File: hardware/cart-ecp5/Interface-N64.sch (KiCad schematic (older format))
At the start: 1 part

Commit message: Add basic N64 interface with UltraCIC II
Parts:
- added J?: Conn_01x05, symbol Connector_Generic:Conn_01x05
- added R?: 10k, symbol Device:R
- added RN4, RN5, RN6, RN7, RN8, RN9: 33R, 1%, Resistor_SMD:R_Array_Convex_4x0603, symbol Device:R_Pack04
- added U?: ATtiny25-20SU, Package_SO:SOIJ-8_5.3x5.3mm_P1.27mm, symbol MCU_Microchip_ATtiny:ATtiny25-20SU
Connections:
- net labels added: CIC_MISO, CIC_MOSI, CIC_RESET#, CIC_SCK, N64_CIC_DATA1, N64_CIC_DATA2, P3V3, xN64_AD0, xN64_AD1, xN64_AD10, xN64_AD11, xN64_AD12, xN64_AD13, xN64_AD14, xN64_AD15, xN64_AD2, xN64_AD3, xN64_AD4, xN64_AD5, xN64_AD6, xN64_AD7, xN64_AD8, xN64_AD9, xN64_ALE_H, xN64_ALE_L, xN64_COLD_RESET#, xN64_OS_EVENT#, xN64_READ#, xN64_WRITE#
- net labels removed: N64_12V, N64_AUDIO_L, N64_AUDIO_R, N64_S_DAT
- wire segments 64 -> 96
- no-connect marks 0 -> 10
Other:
- moved on the sheet: J?

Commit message: First pass annotation and footprint assignment complete
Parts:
- J4: renamed from J?; footprint (none) -> Connector_PinHeader_2.54mm:PinHeader_1x05_P2.54mm_Vertical
- R6: renamed from R?; footprint (none) -> Resistor_SMD:R_0603_1608Metric
- gave numbers to parts that had none: 2
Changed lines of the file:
@@
 $EndDescr
 $Comp
-L ng_n64:N64_Cartridge_Bus J?
+L ng_n64:N64_Cartridge_Bus J3
 U 1 1 5F443545
 P 3000 4050
-F 0 "J?" H 2450 5800 60  0000 L CNN
+F 0 "J3" H 2450 5800 60  0000 L CNN
 F 1 "N64_Cartridge_Bus" H 2450 2300 60  0000 L CNN
 F 2 "ng_n64:N64_Cartridge_Edge" H 3600 550 60  0001 C CNN
@@
 xN64_ALE_H
 $Comp
-L MCU_Microchip_ATtiny:ATtiny25-20SU U?
+L MCU_Microchip_ATtiny:ATtiny25-20SU U4
 U 1 1 5F5E9784
 P 7450 4950
-F 0 "U?" H 6921 4996 50  0000 R CNN
+F 0 "U4" H 6921 4996 50  0000 R CNN
 F 1 "ATtiny25-20SU" H 6921 4905 50  0000 R CNN
 F 2 "Package_SO:SOIJ-8_5.3x5.3mm_P1.27mm" H 7450 4950 50  0001 C CIN
@@
 	7450 5550 7450 5650
 $Comp
-L ng_power:GND #PWR?
+L ng_power:GND #PWR013
 U 1 1 5F5EFD38
 P 2200 5750
-F 0 "#PWR?" H 2200 5500 50  0001 C CNN
+F 0 "#PWR013" H 2200 5500 50  0001 C CNN
 F 1 "GND" H 2203 5624 50  0000 C CNN
 F 2 "" H 2100 5400 50  0001 C CNN
@@
 $EndComp
 $Comp
-L ng_power:GND #PWR?
+L ng_power:GND #PWR015
 U 1 1 5F5F0698
 P 7450 5650
-F 0 "#PWR?" H 7450 5400 50  0001 C CNN
+F 0 "#PWR015" H 7450 5400 50  0001 C CNN
 F 1 "GND" H 7453 5524 50  0000 C CNN
 F 2 "" H 7350 5300 50  0001 C CNN
@@
 	6750 4650 6750 5250
 $Comp
-L ng_power:GND #PWR?
+L ng_power:GND #PWR014
 U 1 1 5F607950
 P 6750 5650
-F 0 "#PWR?" H 6750 5400 50  0001 C CNN
+F 0 "#PWR014" H 6750 5400 50  0001 C CNN
 F 1 "GND" H 6753 5524 50  0000 C CNN
 F 2 "" H 6650 5300 50  0001 C CNN
@@
 CIC_MISO
 $Comp
-L Device:R R?
+L Device:R R6
 U 1 1 5F61BC6C
 P 6750 5400
-F 0 "R?" H 6680 5354 50  0000 R CNN
+F 0 "R6" H 6680 5354 50  0000 R CNN
 F 1 "10k" H 6680 5445 50  0000 R CNN
-F 2 "" V 6680 5400 50  0001 C CNN
+F 2 "Resistor_SMD:R_0603_1608Metric" V 6680 5400 50  0001 C CNN
 F 3 "~" H 6750 5400 50  0001 C CNN
 	1    6750 5400
@@
 NoConn ~ 6850 5050
 $Comp
-L Connector_Generic:Conn_01x05 J?
+L Connector_Generic:Conn_01x05 J4
 U 1 1 5F631439
 P 9700 4950
-F 0 "J?" H 9780 4992 50  0000 L CNN
+F 0 "J4" H 9780 4992 50  0000 L CNN
 F 1 "Conn_01x05" H 9780 4901 50  0000 L CNN
-F 2 "" H 9700 4950 50  0001 C CNN
+F 2 "Connector_PinHeader_2.54mm:PinHeader_1x05_P2.54mm_Vertical" H 9700 4950 50  0001 C CNN
 F 3 "~" H 9700 4950 50  0001 C CNN
 	1    9700 4950
@@
 	9400 4750 9400 5250
 $Comp
-L ng_power:GND #PWR?
+L ng_power:GND #PWR016
 U 1 1 5F634AA1
 P 9400 5250
-F 0 "#PWR?" H 9400 5000 50  0001 C CNN
+F 0 "#PWR016" H 9400 5000 50  0001 C CNN
 F 1 "GND" H 9403 5124 50  0000 C CNN
 F 2 "" H 9300 4900 50  0001 C CNN

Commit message: Initial placement pass
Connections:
- net N64_AD0: now also RN4.5 (R4.2); no longer RN4.7 (R2.2)
- net N64_AD1: now also RN4.7 (R2.2); no longer RN4.5 (R4.2)
- net N64_AD10: now also RN5.8 (R1.2); no longer RN5.6 (R3.2)
- net N64_AD11: now also RN5.6 (R3.2); no longer RN5.8 (R1.2)
- net N64_AD12: now also RN6.8 (R1.2); no longer RN6.6 (R3.2)
- net N64_AD13: now also RN6.6 (R3.2); no longer RN6.8 (R1.2)
- net N64_AD14: now also RN4.8 (R1.2); no longer RN4.6 (R3.2)
- net N64_AD15: now also RN4.6 (R3.2); no longer RN4.8 (R1.2)
- net N64_AD2: now also RN6.5 (R4.2); no longer RN6.7 (R2.2)
- net N64_AD3: now also RN6.7 (R2.2); no longer RN6.5 (R4.2)
- net N64_AD4: now also RN5.5 (R4.2); no longer RN5.7 (R2.2)
- net N64_AD5: now also RN5.7 (R2.2); no longer RN5.5 (R4.2)
- net N64_AD6: now also RN7.5 (R4.2); no longer RN7.7 (R2.2)
- net N64_AD7: now also RN7.7 (R2.2); no longer RN7.5 (R4.2)
- net N64_AD8: now also RN7.8 (R1.2); no longer RN7.6 (R3.2)
- net N64_AD9: now also RN7.6 (R3.2); no longer RN7.8 (R1.2)
- net N64_ALE_H: now also RN8.7 (R2.2); no longer RN8.5 (R4.2)
- net N64_ALE_L: now also RN8.5 (R4.2); no longer RN8.8 (R1.2)
- net N64_OS_EVENT#: now also RN9.6 (R3.2); no longer RN9.8 (R1.2)
- net N64_READ#: now also RN8.8 (R1.2); no longer RN8.6 (R3.2)
- net N64_S_CLK: now also RN9.5 (R4.2); no longer J3.19 (S_CLK)
- net N64_WRITE#: now also RN8.6 (R3.2); no longer RN8.7 (R2.2)
- net xN64_AD0: now also RN4.4 (R4.1); no longer RN4.2 (R2.1)
- net xN64_AD1: now also RN4.2 (R2.1); no longer RN4.4 (R4.1)
- net xN64_AD10: now also RN5.1 (R1.1); no longer RN5.3 (R3.1)
- net xN64_AD11: now also RN5.3 (R3.1); no longer RN5.1 (R1.1)
- net xN64_AD12: now also RN6.1 (R1.1); no longer RN6.3 (R3.1)
- net xN64_AD13: now also RN6.3 (R3.1); no longer RN6.1 (R1.1)
- net xN64_AD14: now also RN4.1 (R1.1); no longer RN4.3 (R3.1)
- net xN64_AD15: now also RN4.3 (R3.1); no longer RN4.1 (R1.1)
- net xN64_AD2: now also RN6.4 (R4.1); no longer RN6.2 (R2.1)
- net xN64_AD3: now also RN6.2 (R2.1); no longer RN6.4 (R4.1)
- net xN64_AD4: now also RN5.4 (R4.1); no longer RN5.2 (R2.1)
- net xN64_AD5: now also RN5.2 (R2.1); no longer RN5.4 (R4.1)
- net xN64_AD6: now also RN7.4 (R4.1); no longer RN7.2 (R2.1)
- net xN64_AD7: now also RN7.2 (R2.1); no longer RN7.4 (R4.1)
- net xN64_AD8: now also RN7.1 (R1.1); no longer RN7.3 (R3.1)
- net xN64_AD9: now also RN7.3 (R3.1); no longer RN7.1 (R1.1)
- net xN64_ALE_H: now also RN8.2 (R2.1); no longer RN8.4 (R4.1)
- net xN64_ALE_L: now also RN8.4 (R4.1); no longer RN8.1 (R1.1)
- net xN64_OS_EVENT#: now also RN9.3 (R3.1); no longer RN9.1 (R1.1)
- net xN64_READ#: now also RN8.1 (R1.1); no longer RN8.3 (R3.1)
- net xN64_WRITE#: now also RN8.3 (R3.1); no longer RN8.2 (R2.1)
- net xN64_S_CLK: now reaches RN9.4 (R4.1)
- net xN64_S_CLK: now also J3.19 (S_CLK)
- net xN64_S_DAT: now reaches J3.21 (S_DAT)
- net xN64_S_DAT: now also RN9.1 (R1.1)
- new net N64_S_DAT: RN9.8 (R1.2)
- no-connect marks 10 -> 5
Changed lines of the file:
@@
 AR Path="/5F1CD155" Ref="RN?"  Part="1"
 AR Path="/5F133F50/5F1CD155" Ref="RN4"  Part="1"
-AR Path="/5F43B1FD/5F1CD155" Ref="RN4"  Part="1"
-F 0 "RN4" V 6683 2100 50  0000 C CNN
+AR Path="/5F43B1FD/5F1CD155" Ref="RN1"  Part="1"
+F 0 "RN1" V 6683 2100 50  0000 C CNN
 F 1 "33R, 1%" V 6774 2100 50  0000 C CNN
 F 2 "Resistor_SMD:R_Array_Convex_4x0603" V 7375 2100 50  0001 C CNN
@@
 AR Path="/5F1CD15B" Ref="RN?"  Part="1"
 AR Path="/5F133F50/5F1CD15B" Ref="RN6"  Part="1"
-AR Path="/5F43B1FD/5F1CD15B" Ref="RN6"  Part="1"
-F 0 "RN6" V 6683 2800 50  0000 C CNN
+AR Path="/5F43B1FD/5F1CD15B" Ref="RN2"  Part="1"
+F 0 "RN2" V 6683 2800 50  0000 C CNN
 F 1 "33R, 1%" V 6774 2800 50  0000 C CNN
 F 2 "Resistor_SMD:R_Array_Convex_4x0603" V 7375 2800 50  0001 C CNN
@@
 AR Path="/5F1CD161" Ref="RN?"  Part="1"
 AR Path="/5F133F50/5F1CD161" Ref="RN8"  Part="1"
-AR Path="/5F43B1FD/5F1CD161" Ref="RN8"  Part="1"
-F 0 "RN8" V 6683 3500 50  0000 C CNN
+AR Path="/5F43B1FD/5F1CD161" Ref="RN3"  Part="1"
+F 0 "RN3" V 6683 3500 50  0000 C CNN
 F 1 "33R, 1%" V 6774 3500 50  0000 C CNN
 F 2 "Resistor_SMD:R_Array_Convex_4x0603" V 7375 3500 50  0001 C CNN
@@
 AR Path="/5F1CD167" Ref="RN?"  Part="1"
 AR Path="/5F133F50/5F1CD167" Ref="RN5"  Part="1"
-AR Path="/5F43B1FD/5F1CD167" Ref="RN5"  Part="1"
-F 0 "RN5" V 8533 2100 50  0000 C CNN
+AR Path="/5F43B1FD/5F1CD167" Ref="RN4"  Part="1"
+F 0 "RN4" V 8533 2100 50  0000 C CNN
 F 1 "33R, 1%" V 8624 2100 50  0000 C CNN
 F 2 "Resistor_SMD:R_Array_Convex_4x0603" V 9225 2100 50  0001 C CNN
@@
 AR Path="/5F1CD16D" Ref="RN?"  Part="1"
 AR Path="/5F133F50/5F1CD16D" Ref="RN7"  Part="1"
-AR Path="/5F43B1FD/5F1CD16D" Ref="RN7"  Part="1"
-F 0 "RN7" V 8533 2800 50  0000 C CNN
+AR Path="/5F43B1FD/5F1CD16D" Ref="RN5"  Part="1"
+F 0 "RN5" V 8533 2800 50  0000 C CNN
 F 1 "33R, 1%" V 8624 2800 50  0000 C CNN
 F 2 "Resistor_SMD:R_Array_Convex_4x0603" V 9225 2800 50  0001 C CNN
@@
 AR Path="/5F1CD183" Ref="RN?"  Part="1"
 AR Path="/5F133F50/5F1CD183" Ref="RN9"  Part="1"
-AR Path="/5F43B1FD/5F1CD183" Ref="RN9"  Part="1"
-F 0 "RN9" V 8533 3500 50  0000 C CNN
+AR Path="/5F43B1FD/5F1CD183" Ref="RN6"  Part="1"
+F 0 "RN6" V 8533 3500 50  0000 C CNN
 F 1 "33R, 1%" V 8624 3500 50  0000 C CNN
 F 2 "Resistor_SMD:R_Array_Convex_4x0603" V 9225 3500 50  0001 C CNN
@@
 	0    1    1    0
 $EndComp
+Text GLabel 7300 2200 2    50   Input ~ 0
+N64_AD0
+Text GLabel 7300 2100 2    50   Input ~ 0
+N64_AD15
+Text GLabel 7300 1900 2    50   Input ~ 0
+N64_AD14
 Text GLabel 7300 2000 2    50   Input ~ 0
-N64_AD0
-Text GLabel 7300 1900 2    50   Input ~ 0
-N64_AD15
-Text GLabel 7300 2100 2    50   Input ~ 0
-N64_AD14
-Text GLabel 7300 2200 2    50   Input ~ 0
 N64_AD1
+Text GLabel 7300 2900 2    50   Input ~ 0
+N64_AD2
 Text GLabel 7300 2700 2    50   Input ~ 0
-N64_AD2
-Text GLabel 7300 2900 2    50   Input ~ 0
 N64_AD3
+Text GLabel 7300 3600 2    50   Input ~ 0
+N64_ALE_L
+Text GLabel 7300 3400 2    50   Input ~ 0
+N64_ALE_H
+Text GLabel 7300 3500 2    50   Input ~ 0
+N64_WRITE#
 Text GLabel 7300 3300 2    50   Input ~ 0
-N64_ALE_L
-Text GLabel 7300 3600 2    50   Input ~ 0
-N64_ALE_H
-Text GLabel 7300 3400 2    50   Input ~ 0
-N64_WRITE#
-Text GLabel 7300 3500 2    50   Input ~ 0
 N64_READ#
+Text GLabel 7300 2800 2    50   Input ~ 0
+N64_AD13
 Text GLabel 7300 2600 2    50   Input ~ 0
-N64_AD13
-Text GLabel 7300 2800 2    50   Input ~ 0
 N64_AD12
+Text GLabel 9150 2100 2    50   Input ~ 0
+N64_AD11
 Text GLabel 9150 1900 2    50   Input ~ 0
-N64_AD11
-Text GLabel 9150 2100 2    50   Input ~ 0
 N64_AD10
+Text GLabel 9150 2800 2    50   Input ~ 0
+N64_AD9
 Text GLabel 9150 2600 2    50   Input ~ 0
-N64_AD9
-Text GLabel 9150 2800 2    50   Input ~ 0
 N64_AD8
 Text GLabel 9150 3400 2    50   Input ~ 0
 N64_COLD_RESET#
 Text GLabel 9150 3300 2    50   Input ~ 0
-N64_OS_EVENT#
+N64_S_DAT
+Text GLabel 9150 2200 2    50   Input ~ 0
+N64_AD4
 Text GLabel 9150 2000 2    50   Input ~ 0
-N64_AD4
-Text GLabel 9150 2200 2    50   Input ~ 0
 N64_AD5
+Text GLabel 9150 2900 2    50   Input ~ 0
+N64_AD6
 Text GLabel 9150 2700 2    50   Input ~ 0
-N64_AD6
-Text GLabel 9150 2900 2    50   Input ~ 0
 N64_AD7
-NoConn ~ 8750 3600
-NoConn ~ 8750 3500
-NoConn ~ 9150 3500
-NoConn ~ 9150 3600
 NoConn ~ 3700 5550
 NoConn ~ 3700 5650
@@
 xN64_WRITE#
 Text Label 3800 4750 0    50   ~ 0
-N64_S_CLK
+xN64_S_CLK
 Text Label 3800 4950 0    50   ~ 0
 xN64_COLD_RESET#
@@
 Text Label 3800 5350 0    50   ~ 0
 N64_CIC_DATA2
-NoConn ~ 3700 4650
 NoConn ~ 2300 2950
 NoConn ~ 2300 3050
@@
 Wire Wire Line
 	6900 3600 6800 3600
+Text Label 6800 2100 2    50   ~ 0
+xN64_AD15
+Text Label 6800 2200 2    50   ~ 0
+xN64_AD0
 Text Label 6800 1900 2    50   ~ 0
-xN64_AD15
+xN64_AD14
 Text Label 6800 2000 2    50   ~ 0
-xN64_AD0
-Text Label 6800 2100 2    50   ~ 0
-xN64_AD14
-Text Label 6800 2200 2    50   ~ 0
 xN64_AD1
+Text Label 6800 2800 2    50   ~ 0
+xN64_AD13
+Text Label 6800 2900 2    50   ~ 0
+xN64_AD2
 Text Label 6800 2600 2    50   ~ 0
-xN64_AD13
+xN64_AD12
 Text Label 6800 2700 2    50   ~ 0
-xN64_AD2
-Text Label 6800 2800 2    50   ~ 0
-xN64_AD12
-Text Label 6800 2900 2    50   ~ 0
 xN64_AD3
+Text Label 8650 2100 2    50   ~ 0
+xN64_AD11
+Text Label 8650 2200 2    50   ~ 0
+xN64_AD4
 Text Label 8650 1900 2    50   ~ 0
-xN64_AD11
+xN64_AD10
 Text Label 8650 2000 2    50   ~ 0
-xN64_AD4
-Text Label 8650 2100 2    50   ~ 0
-xN64_AD10
-Text Label 8650 2200 2    50   ~ 0
 xN64_AD5
 Wire Wire Line
@@
 Wire Wire Line
 	8750 3400 8650 3400
+Text Label 8650 2900 2    50   ~ 0
+xN64_AD6
+Text Label 8650 2800 2    50   ~ 0
+xN64_AD9
 Text Label 8650 2700 2    50   ~ 0
-xN64_AD6
+xN64_AD7
 Text Label 8650 2600 2    50   ~ 0
-xN64_AD9
-Text Label 8650 2900 2    50   ~ 0
-xN64_AD7
-Text Label 8650 2800 2    50   ~ 0
 xN64_AD8
-Text Label 8650 3300 2    50   ~ 0
+Text Label 8650 3500 2    50   ~ 0
 xN64_OS_EVENT#
 Text Label 8650 3400 2    50   ~ 0
 xN64_COLD_RESET#
+Text Label 6800 3600 2    50   ~ 0
+xN64_ALE_L
+Text Label 6800 3500 2    50   ~ 0
+xN64_WRITE#
 Text Label 6800 3300 2    50   ~ 0
-xN64_ALE_L
+xN64_READ#
 Text Label 6800 3400 2    50   ~ 0
-xN64_WRITE#
-Text Label 6800 3500 2    50   ~ 0
-xN64_READ#
-Text Label 6800 3600 2    50   ~ 0
 xN64_ALE_H
 $Comp
@@
 Text Label 6100 4750 2    50   ~ 0
 N64_CIC_DATA2
-Text Label 6100 4950 2    50   ~ 0
-N64_S_CLK
 Text Label 6100 4850 2    50   ~ 0
 N64_CIC_DATA1
@@
 Text Label 9300 5150 2    50   ~ 0
 CIC_RESET#
+Wire Wire Line
+	3700 4650 3800 4650
+Text Label 3800 4650 0    50   ~ 0
+xN64_S_DAT
+Wire Wire Line
+	8750 3500 8650 3500
+Wire Wire Line
+	8750 3600 8650 3600
+Text GLabel 9150 3600 2    50   Input ~ 0
+N64_S_CLK
+Text GLabel 9150 3500 2    50   Input ~ 0
+N64_OS_EVENT#
+Text Label 8650 3300 2    50   ~ 0
+xN64_S_DAT
+Text Label 8650 3600 2    50   ~ 0
+xN64_S_CLK
+Text GLabel 6100 4950 0    50   Input ~ 0
+N64_S_CLK
 $EndSCHEMATC

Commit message: Shrink smallest passive to 0402
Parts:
- R6: footprint Resistor_SMD:R_0603_1608Metric -> Resistor_SMD:R_0402_1005Metric
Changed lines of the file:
@@
 F 0 "R6" H 6680 5354 50  0000 R CNN
 F 1 "10k" H 6680 5445 50  0000 R CNN
-F 2 "Resistor_SMD:R_0603_1608Metric" V 6680 5400 50  0001 C CNN
+F 2 "Resistor_SMD:R_0402_1005Metric" V 6680 5400 50  0001 C CNN
 F 3 "~" H 6750 5400 50  0001 C CNN
 	1    6750 5400

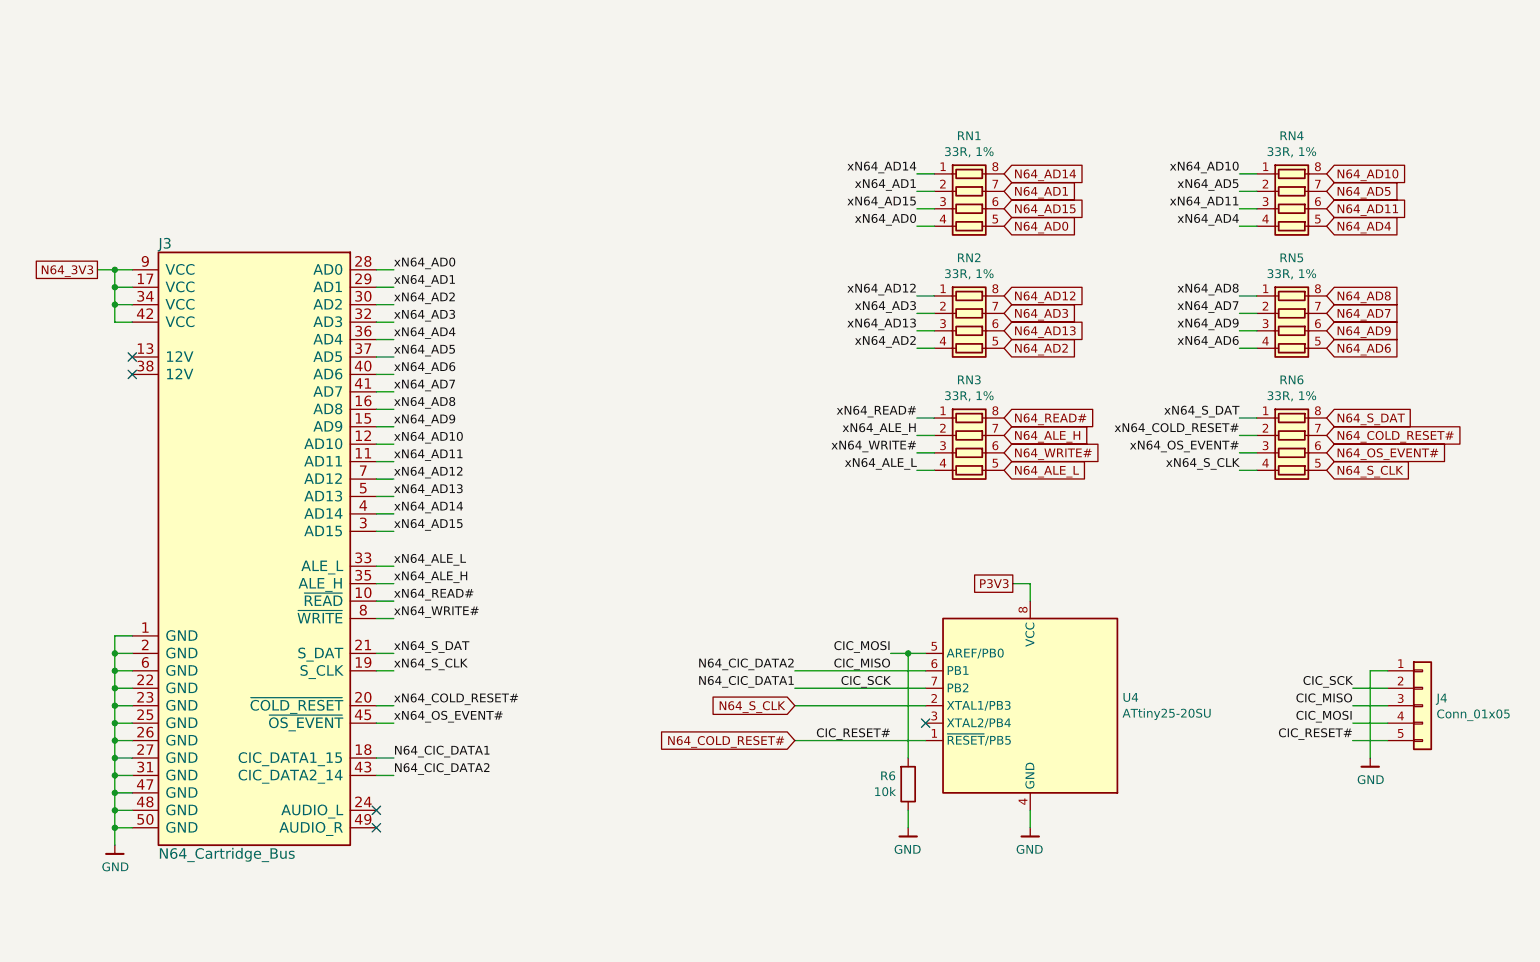
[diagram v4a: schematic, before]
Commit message: Refine placement to make room for power management
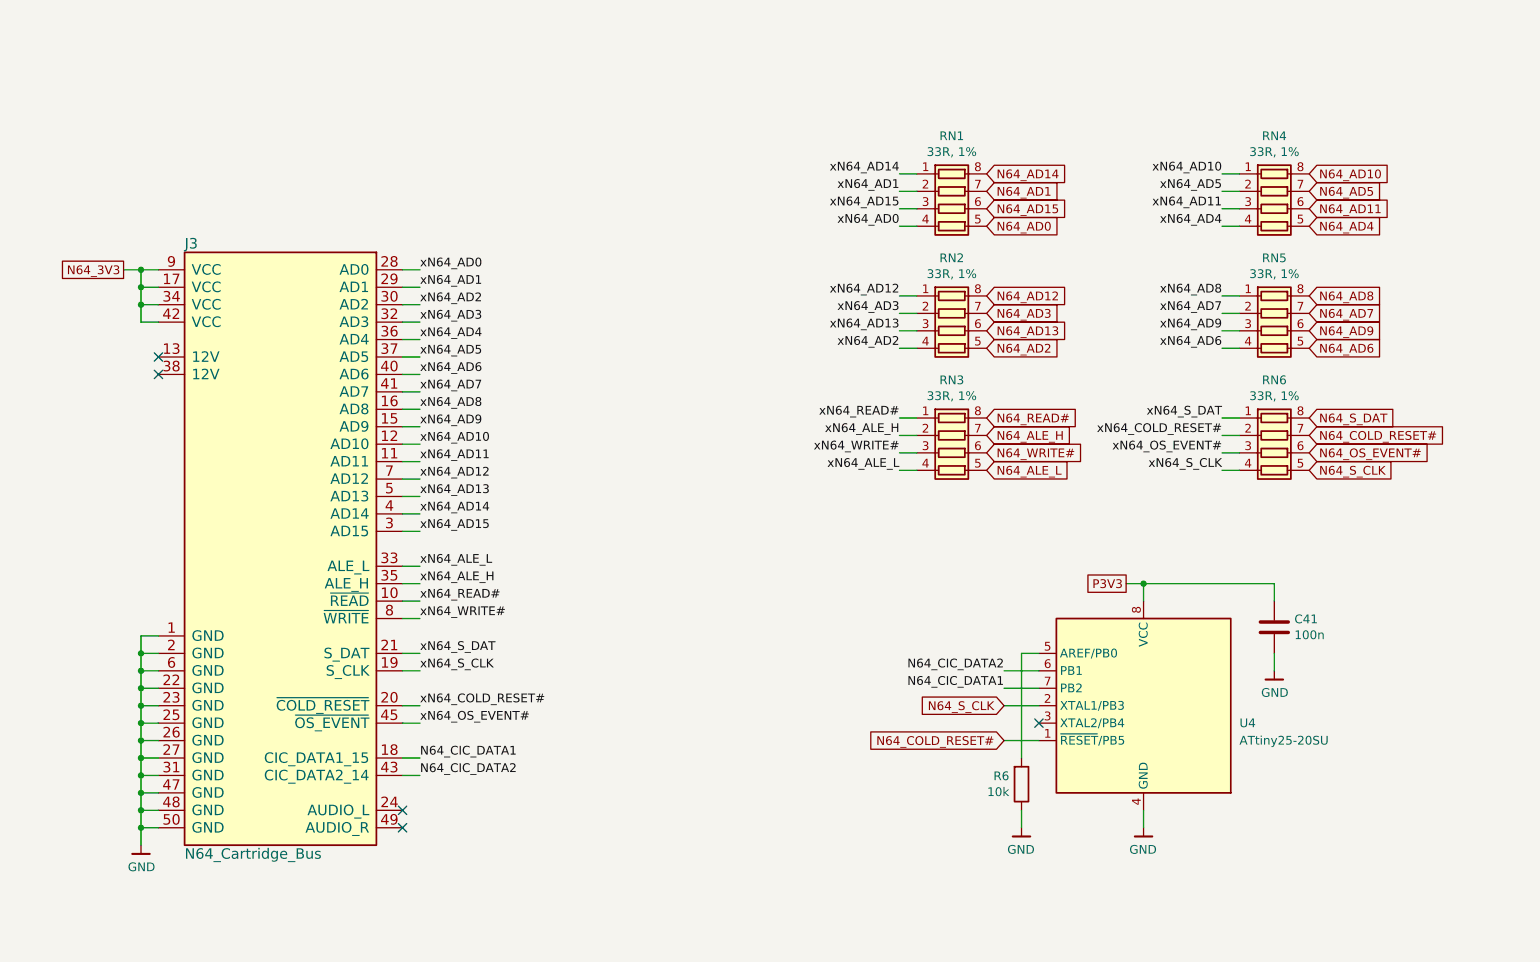
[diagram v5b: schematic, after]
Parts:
- removed J4: Conn_01x05, Connector_PinHeader_2.54mm:PinHeader_1x05_P2.54mm_Vertical, symbol Connector_Generic:Conn_01x05
- added C41: 100n, Capacitor_SMD:C_0402_1005Metric, symbol Device:C
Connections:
- net GND: now also C41.2
- net P3V3: now also C41.1
- net CIC_MISO renamed N64_CIC_DATA2
- net CIC_MOSI: no longer names the net of R6.2, U4.5 (AREF/PB0)
- net CIC_SCK renamed N64_CIC_DATA1
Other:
- moved on the sheet: J3, R6, RN1, RN2, RN3, RN4, RN5, RN6, U4
